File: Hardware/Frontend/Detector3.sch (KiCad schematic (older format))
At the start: 27 parts, among them J5 Conn_Coaxial, U7 OPA145ID, U8 OPA145ID, U9 OPA145ID

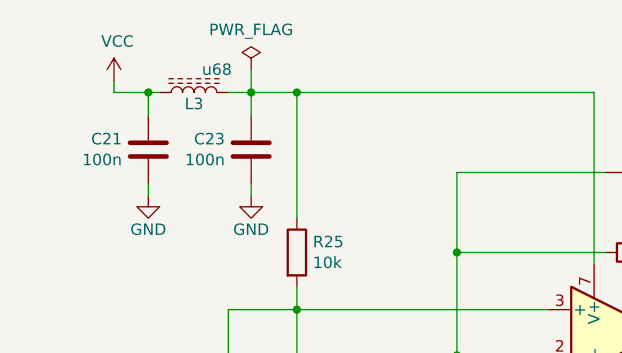
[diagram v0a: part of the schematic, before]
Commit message: add bom
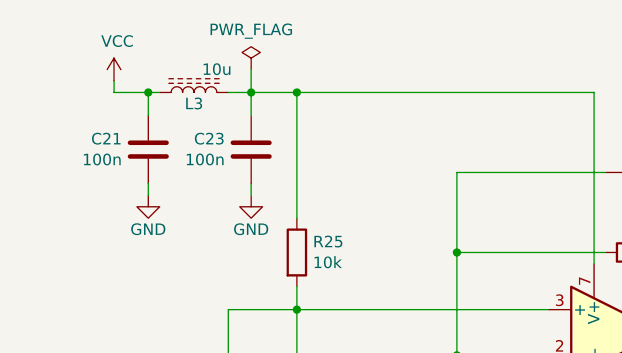
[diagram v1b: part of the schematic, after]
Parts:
- L3: value u68 -> 10u
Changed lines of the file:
@@
 AR Path="/6126C995/61420429" Ref="L3"  Part="1"
 F 0 "L3" V 2800 2550 50  0000 C CNN
-F 1 "u68" V 2950 2650 50  0000 C CNN
+F 1 "10u" V 2950 2650 50  0000 C CNN
 F 2 "Inductor_SMD:L_0805_2012Metric" H 2850 2550 50  0001 C CNN
 F 3 "" H 2850 2550 50  0001 C CNN
